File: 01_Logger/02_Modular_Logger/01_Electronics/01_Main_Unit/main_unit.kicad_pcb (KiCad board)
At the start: 4 copper layers, 114.4 x 72.1 mm, 166 parts, among them IC501 BQ24618, IC801 BQ40Z80, J101 SFMC-107-01-L-D, J102 FTS-107-01-F-D, J301 Conn_01x02, J302 Conn_02x04_Counter_Clockwise, J303 Conn_01x02, J304 Conn_02x02_Odd_Even, J501 Conn_01x02, J502 Conn_01x02_Female, J701 Micro_SD_Card_Det, J801 Conn_01x02_Male, J802 Conn_01x05_Male, K501 SISH101DN-T1-GE3, K502 SISH101DN-T1-GE3, K503 SiS412DN, K504 SiS412DN, K505 SISH101DN-T1-GE3, K801 2N7002KW, K802 CSD18540Q5B, K803 DMP6023LSS-13, K804 CSD18540Q5B, Q301 BSS138, Q601 BSS123, Q602 IRLML6401, Q603 BSS123, Q604 IRLML6401, SW301 SW_Push, SW801 SW_Push, U301 MAX16125WTEG00+T, U302 ESP32-S3-WROOM-1U, U303 DS3231MZ, U601 SPBW06F-12, U602 OKI-78SR-3.3_1.5-W36-C, U603 OKI-78SR-5_1.5-W36-C, Y301 Crystal

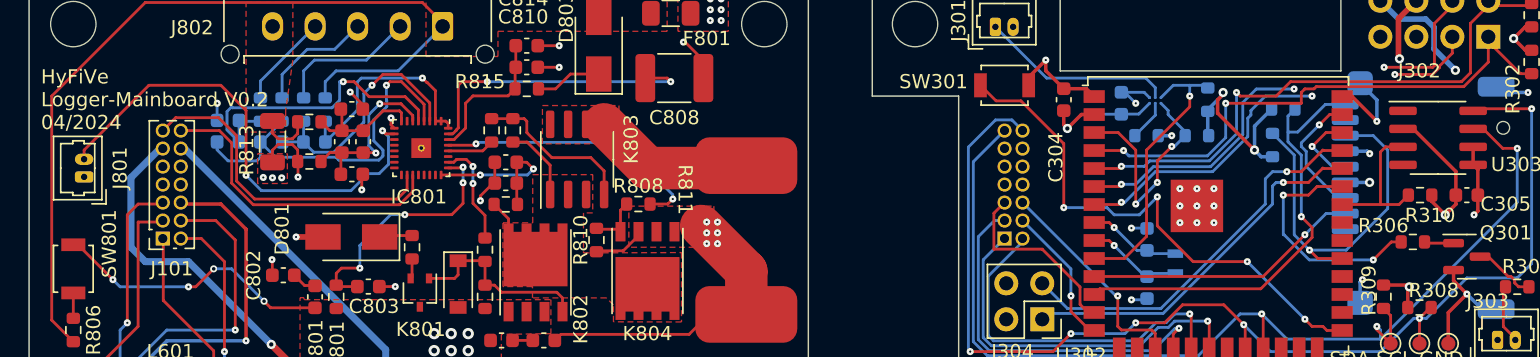
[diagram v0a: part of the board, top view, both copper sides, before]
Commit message: update Electronics for Modular_Logger
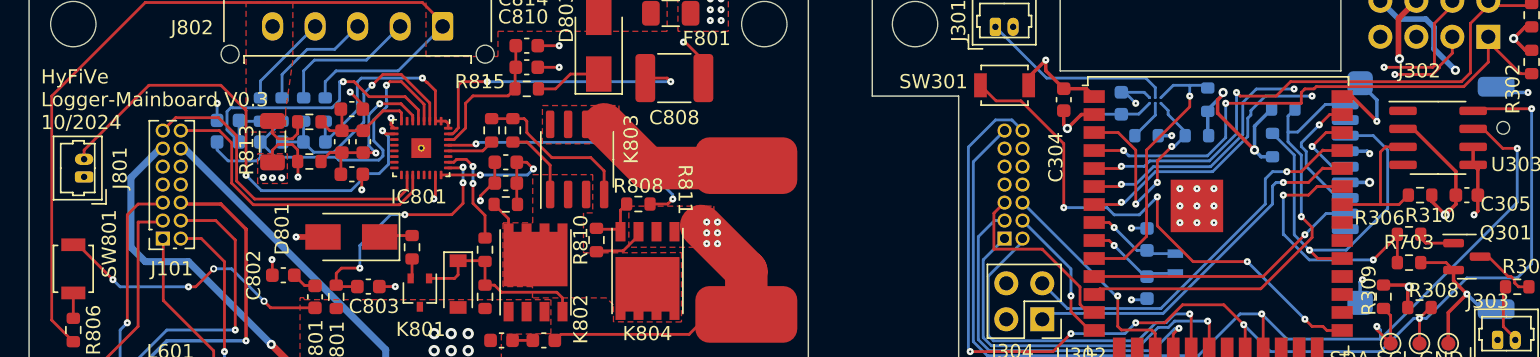
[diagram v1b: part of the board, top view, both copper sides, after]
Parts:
- added R703: 1M, Resistor_SMD:R_0603_1608Metric, F.Cu at (197.4, 98.1)
- Q602, Q604: value IRLML6401 -> IRLML5203TRPBF
- R501: value 2 -> 100
- R522: value 348k -> 357k
- R806: value 10k -> 51
- moved R306 0.60 mm to (197.4, 96.1)
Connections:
- IC801 pad 23: unconnected-(IC801-Pad23) -> GND
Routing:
- net GND: track 123.4 -> 127.7 mm, vias 73 -> 74
- net /MPU/LED_STATUS: track 16.8 -> 18.8 mm
- net Net-(Q301-G): track 1.96 -> 2.73 mm
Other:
- board text added: "HyFiVe Logger-MPU-Board V0.3 10/2024"
- board text added: "HyFiVe Logger-Mainboard V0.3 10/2024"
- board text removed: "HyFiVe Logger-MPU-Board V0.2 04/2024"
- board text removed: "HyFiVe Logger-Mainboard V0.2 04/2024"
